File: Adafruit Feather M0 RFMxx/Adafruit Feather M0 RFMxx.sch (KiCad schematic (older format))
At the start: 41 parts, among them SW1 SPST_TACT-KMR2, U1 2MB Flash, U2 AP2112K-3.3, U3 MCP73831T-2ACI/OT, U4 RFM69HCW, X1 JSTPH, X2 32.768, X3 microUSB, X4 uFL

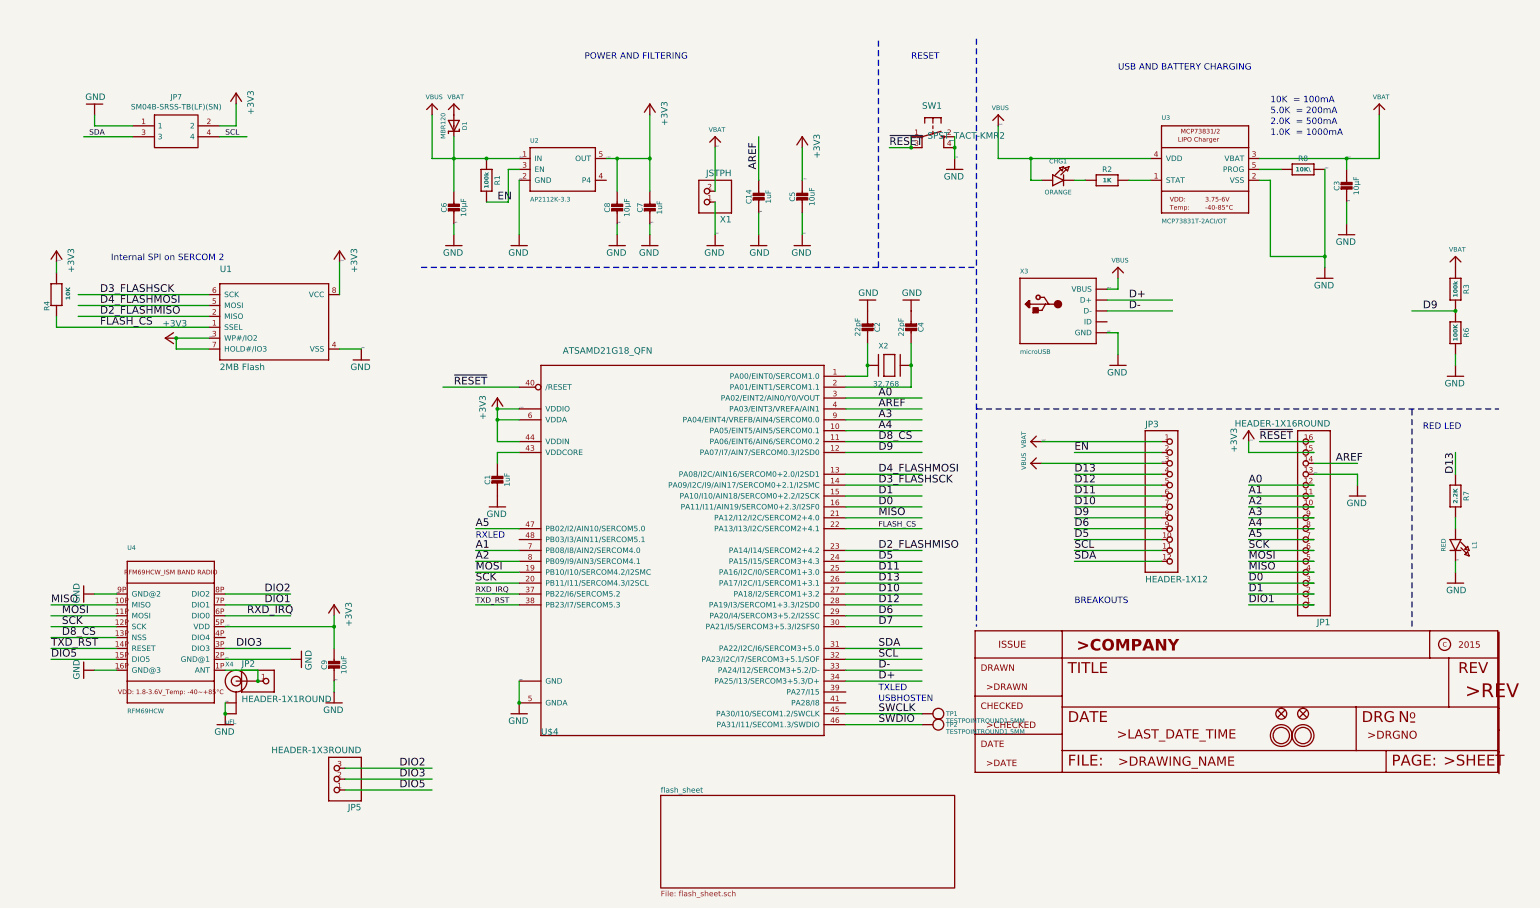
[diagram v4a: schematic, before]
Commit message: Parts mostly added. Need to confirm footprints. Before eliminating RFM parts.
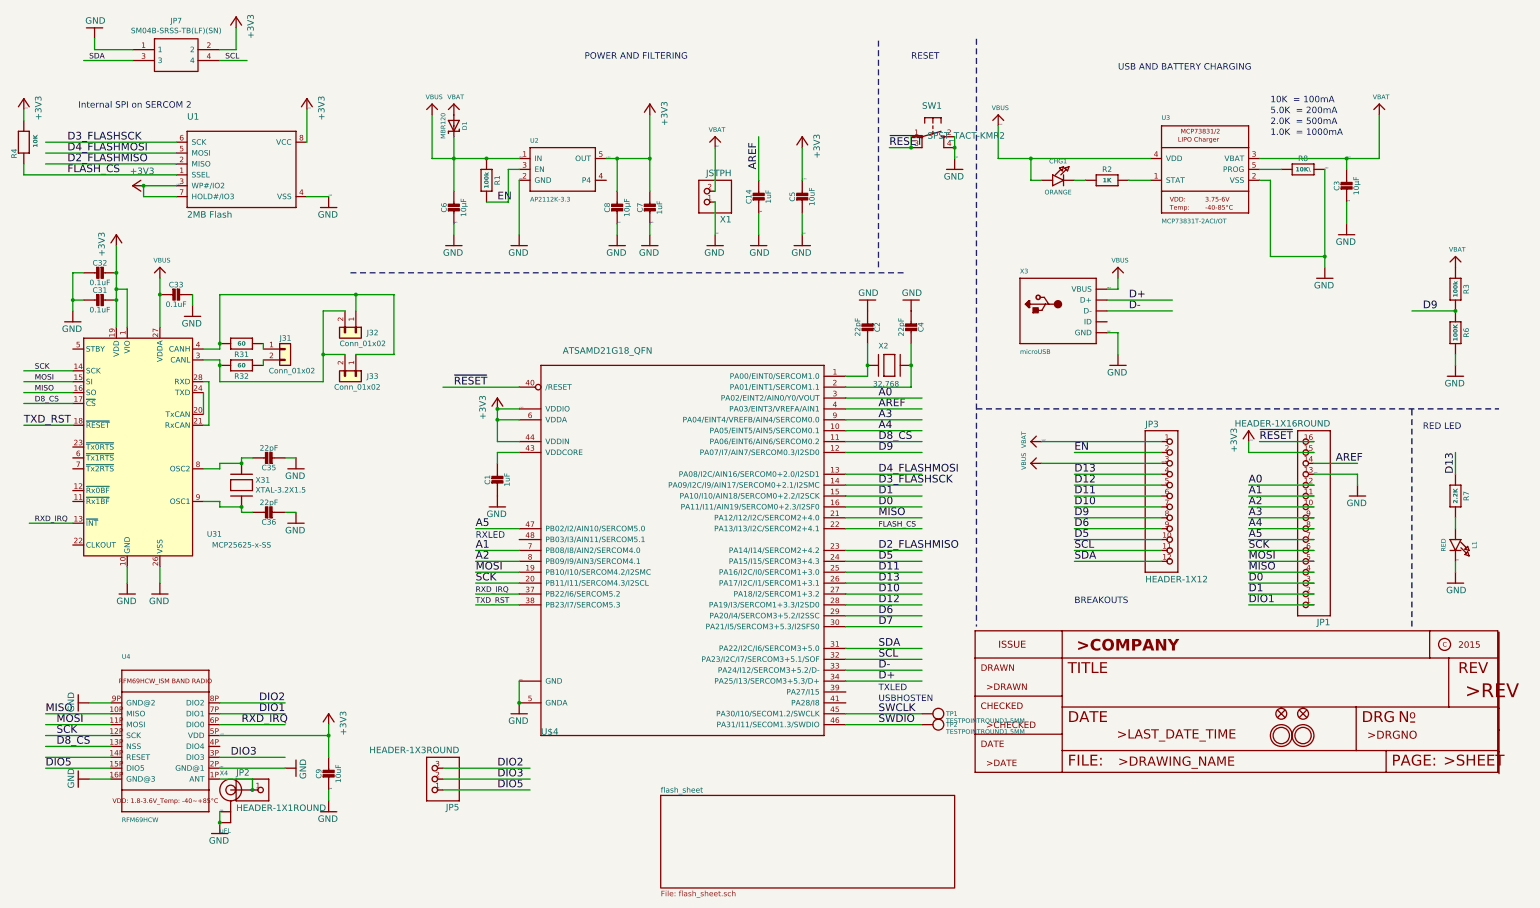
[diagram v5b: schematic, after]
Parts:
- added C31, C32, C33: 0.1uF, Adafruit Feather M0 RFMxx:0603-NO, symbol Adafruit_Feather_M0_RFMxx-eagle-import:CAP_CERAMIC0603_NO
- added C35, C36: 22pF, Adafruit Feather M0 RFMxx:0603-NO, symbol Adafruit_Feather_M0_RFMxx-eagle-import:CAP_CERAMIC0603_NO
- added J31: Conn_01x02, Socket_Strips:Socket_Strip_Straight_1x02_Pitch2.54mm, symbol Connector_Generic:Conn_01x02
- added J32, J33: Conn_01x02, Pin_Headers:Pin_Header_Straight_1x02_Pitch2.54mm, symbol Connector_Generic:Conn_01x02
- added R31, R32: 60, Adafruit Feather M0 RFMxx:0603-NO, symbol Adafruit_Feather_M0_RFMxx-eagle-import:RESISTOR_0603_NOOUT
- added U31: MCP25625-x-SS, Housings_SSOP:SSOP-28_5.3x10.2mm_Pitch0.65mm, symbol Interface_CAN_LIN:MCP25625-x-SS
- added X31: XTAL-3.2X1.5, Adafruit Feather M0 RFMxx:XTAL3215, symbol Adafruit_Feather_M0_RFMxx-eagle-import:XTAL-3.2X1.5
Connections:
- wire segments 175 -> 230
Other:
- moved on the sheet: C9, JP2, JP5, JP7, R4, U1, U4, X4

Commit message: Eliminated RFM and associated parts. Started to place and route. Must still confirm footprints.
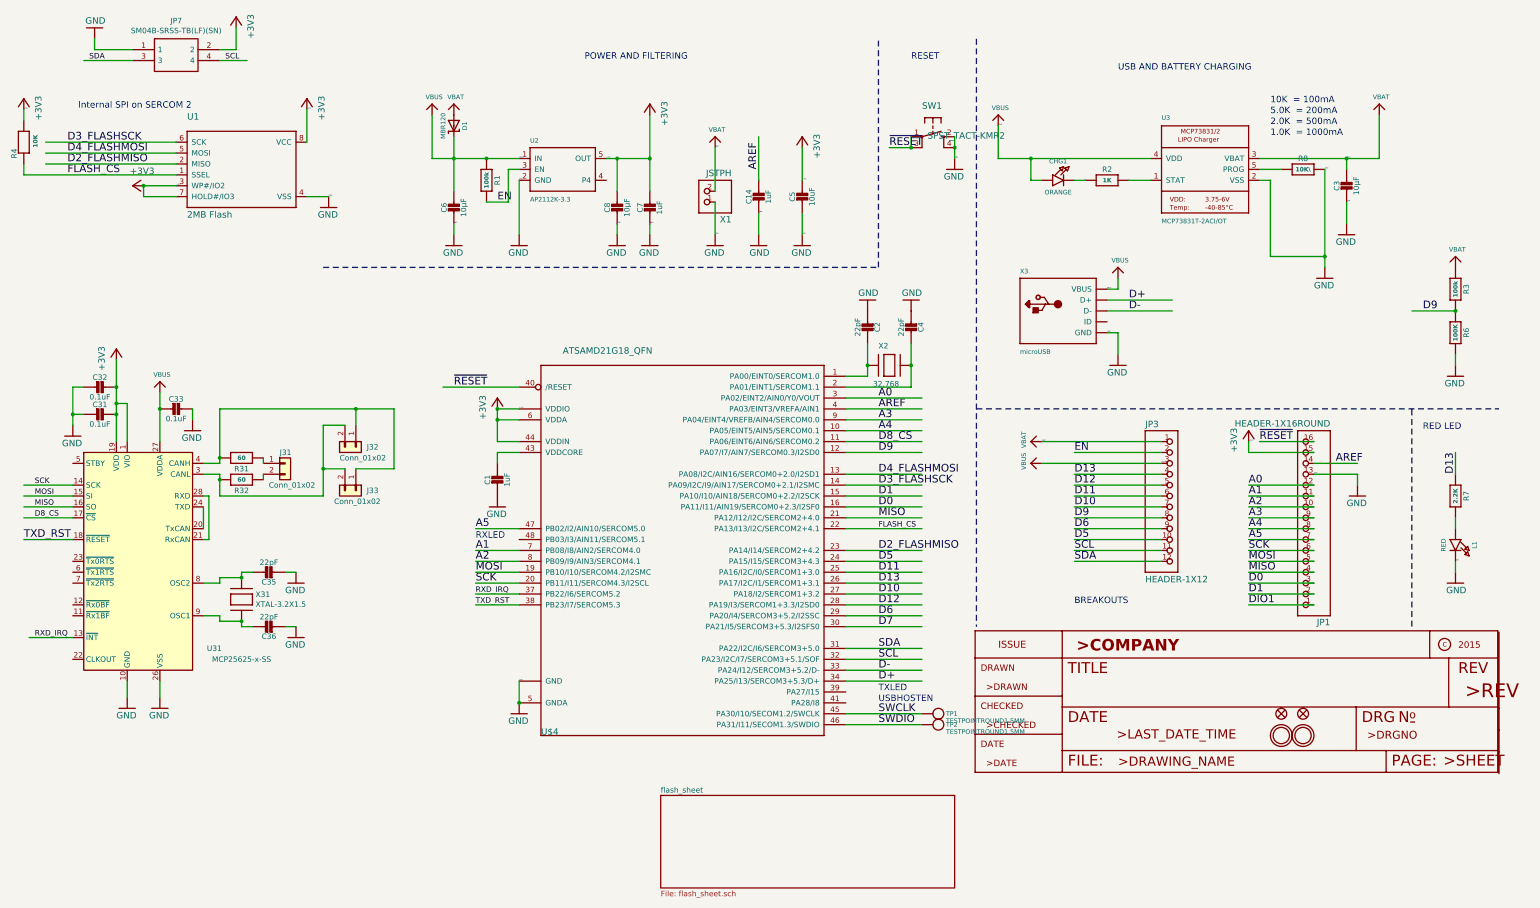
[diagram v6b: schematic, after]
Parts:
- removed C9: 10uF, Adafruit Feather M0 RFMxx:0805-NO, symbol Adafruit_Feather_M0_RFMxx-eagle-import:CAP_CERAMIC0805-NOOUTLINE
- removed JP2: HEADER-1X1ROUND, Adafruit Feather M0 RFMxx:1X01_ROUND, symbol Adafruit_Feather_M0_RFMxx-eagle-import:HEADER-1X1ROUND
- removed JP5: HEADER-1X3ROUND, Adafruit Feather M0 RFMxx:1X03_ROUND, symbol Adafruit_Feather_M0_RFMxx-eagle-import:HEADER-1X3ROUND
- removed U4: RFM69HCW, Adafruit Feather M0 RFMxx:RFMHCW_SMT, symbol Adafruit_Feather_M0_RFMxx-eagle-import:RFM69HCW_SMT
- removed X4: uFL, Adafruit Feather M0 RFMxx:U.FL, symbol Adafruit_Feather_M0_RFMxx-eagle-import:ANTENNA_U.FL
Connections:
- net labels removed: DIO2, DIO3, DIO5
- wire segments 230 -> 207
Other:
- moved on the sheet: C31, C32, C33, C35, C36, J31, J32, J33, R31, R32, U31, X31

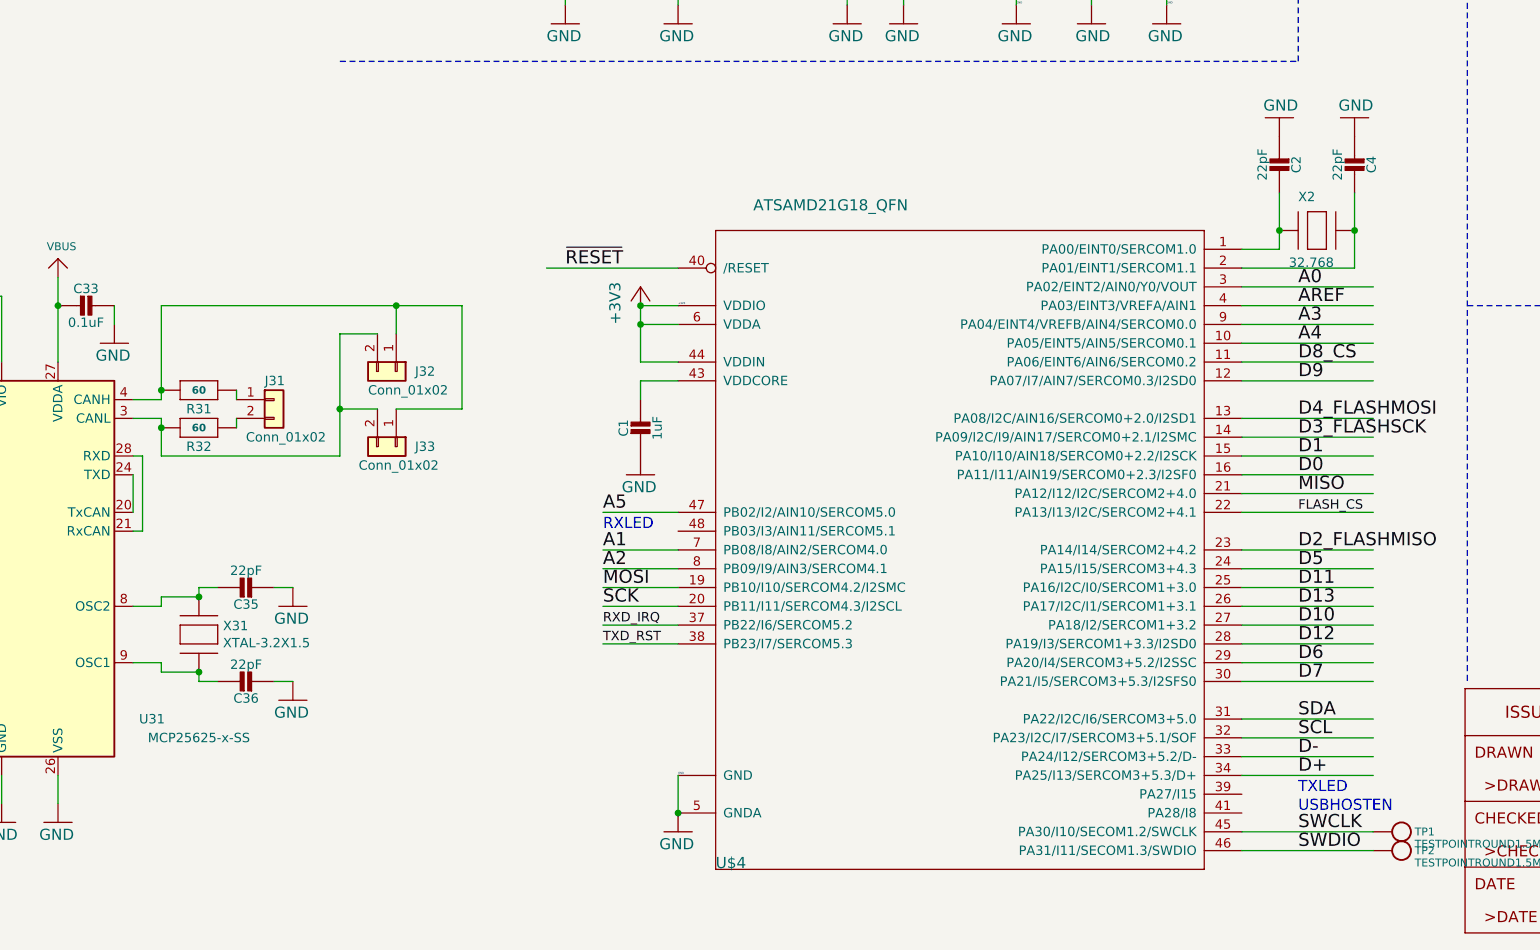
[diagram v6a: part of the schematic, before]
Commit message: Routed, with some remaining errors: - some grounds disconnected - odd error about runner on PAD25 of MCP too close to PAD24. But there is no runner on PAD25 - just the footprint itself.
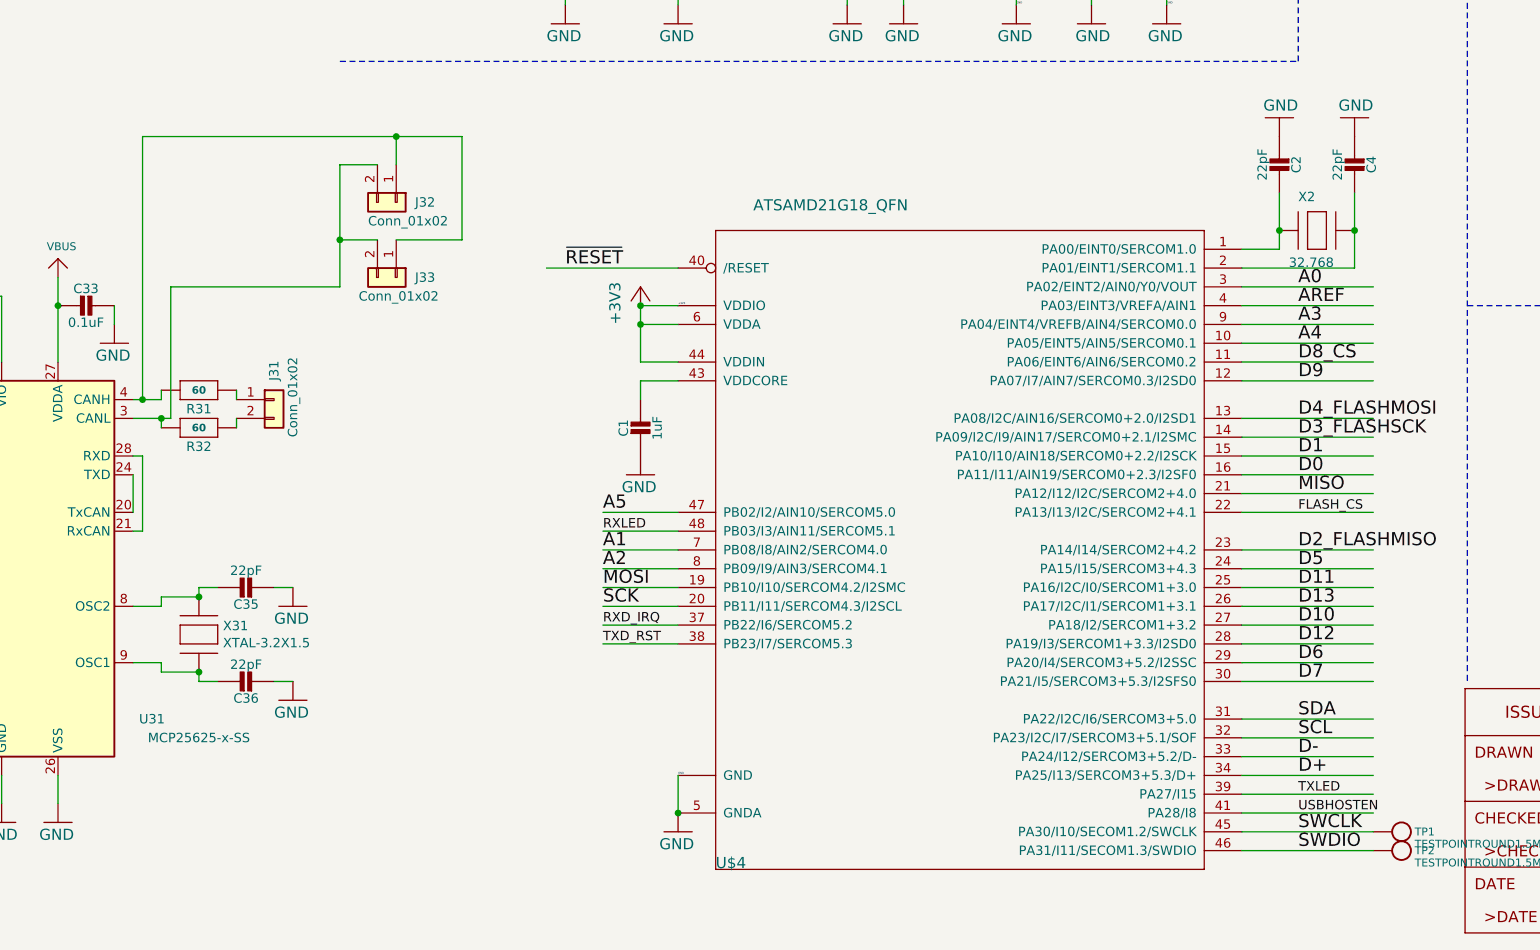
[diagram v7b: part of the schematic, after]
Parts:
- J31: footprint Socket_Strips:Socket_Strip_Straight_1x02_Pitch2.54mm -> Pin_Headers:Pin_Header_Straight_1x02_Pitch2.54mm
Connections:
- net labels added: RXLED, TXLED, USBHOSTEN
- wire segments 207 -> 212
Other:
- note removed: "RXLED"
- note removed: "TXLED"
- note removed: "USBHOSTEN"
- moved on the sheet: J32, J33
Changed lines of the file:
@@
 Text Notes 11900 1600 0    59   ~ 0
 1.0K  = 1000mA
-Text Notes 8300 6700 0    59   ~ 0
-TXLED
-Text Notes 8300 6800 0    59   ~ 0
-USBHOSTEN
-Text Notes 4600 5300 0    59   ~ 0
-RXLED
 Text Notes 10500 1000 0    59   ~ 0
 USB AND BATTERY CHARGING
@@
 	2100 4700 2250 4700
 Wire Wire Line
-	2100 4600 2250 4600
+	2100 4600 2150 4600
 $Comp
 L Adafruit_Feather_M0_RFMxx-eagle-import:+3V3 #+3V0105
@@
 	2250 4700 2250 4750
 Wire Wire Line
-	2250 4100 2250 4550
-Connection ~ 2250 4550
-Wire Wire Line
 	2250 4550 2250 4600
-Connection ~ 2250 4750
-Wire Wire Line
-	2250 4750 2250 4900
 $Comp
 L Adafruit_Feather_M0_RFMxx-eagle-import:CAP_CERAMIC0603_NO C32
@@
 Wire Wire Line
 	900  5300 450  5300
-$Comp
-L Connector_Generic:Conn_01x02 J31
-U 1 1 5C565DEF
-P 2850 4600
-F 0 "J31" H 2800 4700 50  0000 L CNN
-F 1 "Conn_01x02" H 2700 4400 50  0000 L CNN
-F 2 "Socket_Strips:Socket_Strip_Straight_1x02_Pitch2.54mm" H 2850 4600 50  0001 C CNN
-F 3 "~" H 2850 4600 50  0001 C CNN
-	1    2850 4600
-	1    0    0    -1
-$EndComp
 Wire Wire Line
 	2650 4550 2650 4600
@@
 L Connector_Generic:Conn_01x02 J32
 U 1 1 5C593189
-P 3500 4450
-F 0 "J32" V 3500 4550 50  0000 L CNN
-F 1 "Conn_01x02" V 3600 4300 50  0000 L CNN
-F 2 "Pin_Headers:Pin_Header_Straight_1x02_Pitch2.54mm" H 3500 4450 50  0001 C CNN
-F 3 "~" H 3500 4450 50  0001 C CNN
-	1    3500 4450
+P 3500 3550
+F 0 "J32" V 3500 3650 50  0000 L CNN
+F 1 "Conn_01x02" V 3600 3400 50  0000 L CNN
+F 2 "Pin_Headers:Pin_Header_Straight_1x02_Pitch2.54mm" H 3500 3550 50  0001 C CNN
+F 3 "~" H 3500 3550 50  0001 C CNN
+	1    3500 3550
 	0    1    1    0
 $EndComp
@@
 L Connector_Generic:Conn_01x02 J33
 U 1 1 5C5932A2
-P 3500 4850
-F 0 "J33" V 3500 4950 50  0000 L CNN
-F 1 "Conn_01x02" V 3600 4650 50  0000 L CNN
-F 2 "Pin_Headers:Pin_Header_Straight_1x02_Pitch2.54mm" H 3500 4850 50  0001 C CNN
-F 3 "~" H 3500 4850 50  0001 C CNN
-	1    3500 4850
+P 3500 3950
+F 0 "J33" V 3500 4050 50  0000 L CNN
+F 1 "Conn_01x02" V 3600 3750 50  0000 L CNN
+F 2 "Pin_Headers:Pin_Header_Straight_1x02_Pitch2.54mm" H 3500 3950 50  0001 C CNN
+F 3 "~" H 3500 3950 50  0001 C CNN
+	1    3500 3950
 	0    1    1    0
 $EndComp
 Wire Wire Line
-	2250 4900 3200 4900
-Wire Wire Line
-	3500 4100 3500 4250
-Wire Wire Line
-	2250 4100 3500 4100
-Wire Wire Line
-	3500 4100 3850 4100
-Wire Wire Line
-	3850 4100 3850 4650
-Wire Wire Line
-	3850 4650 3500 4650
-Connection ~ 3500 4100
-Wire Wire Line
-	3200 4900 3200 4650
-Wire Wire Line
-	3200 4250 3400 4250
-Wire Wire Line
-	3400 4650 3200 4650
-Connection ~ 3200 4650
-Wire Wire Line
-	3200 4650 3200 4250
+	2300 4000 3200 4000
+Wire Wire Line
+	3500 3200 3500 3350
+Wire Wire Line
+	2150 3200 3500 3200
+Wire Wire Line
+	3500 3200 3850 3200
+Wire Wire Line
+	3850 3200 3850 3750
+Wire Wire Line
+	3850 3750 3500 3750
+Connection ~ 3500 3200
+Wire Wire Line
+	3200 4000 3200 3750
+Wire Wire Line
+	3200 3350 3400 3350
+Wire Wire Line
+	3400 3750 3200 3750
+Connection ~ 3200 3750
+Wire Wire Line
+	3200 3750 3200 3350
 $Comp
 L Adafruit_Feather_M0_RFMxx-eagle-import:GND #U$0107
@@
 	2850 6100 2950 6100
 Connection ~ 1300 3900
+Wire Wire Line
+	5000 5300 4600 5300
+Text Label 4600 5300 0    50   ~ 0
+RXLED
+Wire Wire Line
+	8000 6700 8700 6700
+Wire Wire Line
+	8000 6800 8700 6800
+Text Label 8300 6700 0    50   ~ 0
+TXLED
+Text Label 8300 6800 0    50   ~ 0
+USBHOSTEN
+Wire Wire Line
+	2150 3200 2150 4600
+Connection ~ 2150 4600
+Wire Wire Line
+	2150 4600 2250 4600
+Wire Wire Line
+	2300 4000 2300 4700
+Wire Wire Line
+	2300 4700 2250 4700
+Connection ~ 2250 4700
+$Comp
+L Connector_Generic:Conn_01x02 J31
+U 1 1 5C4611FE
+P 2850 4600
+F 0 "J31" V 2850 4700 50  0000 L CNN
+F 1 "Conn_01x02" V 2950 4400 50  0000 L CNN
+F 2 "Pin_Headers:Pin_Header_Straight_1x02_Pitch2.54mm" H 2850 4600 50  0001 C CNN
+F 3 "~" H 2850 4600 50  0001 C CNN
+	1    2850 4600
+	1    0    0    -1
+$EndComp
 $EndSCHEMATC

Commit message: On MCP25625, added connection from STBY to GND to put device in Normal mode.
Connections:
- wire segments 212 -> 215
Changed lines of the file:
@@
 	1    0    0    -1
 $EndComp
+$Comp
+L Adafruit_Feather_M0_RFMxx-eagle-import:GND #U$?
+U 1 0 5C3CB150
+P 600 4600
+F 0 "#U$?" H 600 4600 50  0001 C CNN
+F 1 "GND" H 500 4500 59  0000 L BNN
+F 2 "" H 600 4600 50  0001 C CNN
+F 3 "" H 600 4600 50  0001 C CNN
+	1    600  4600
+	1    0    0    -1
+$EndComp
+Wire Wire Line
+	900  4600 750  4600
+Wire Wire Line
+	750  4600 750  4500
+Wire Wire Line
+	750  4500 600  4500
 $EndSCHEMATC
